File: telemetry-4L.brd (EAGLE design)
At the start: 69.8 x 22.9 mm, 70 parts, among them SW1 MF-SW-TACT-4.2MM, SW2 PCM12SMTR, U1 ATSAMD21G18A-MUT, U2 SPX3819M5-L-3-0, U3 MCP73831T-2ACI/OT, U4 IRLML6344TRPBF, U5 SIM868, U6 BMP280, U7 MPU-9250, U8 TPS61253YFFR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

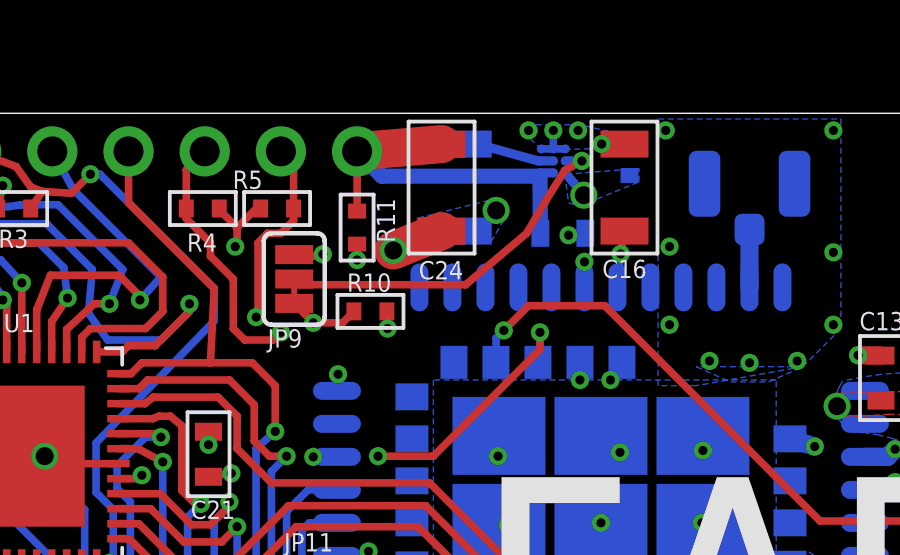
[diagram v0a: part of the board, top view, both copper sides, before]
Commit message: Killed "Servo Power 2" components
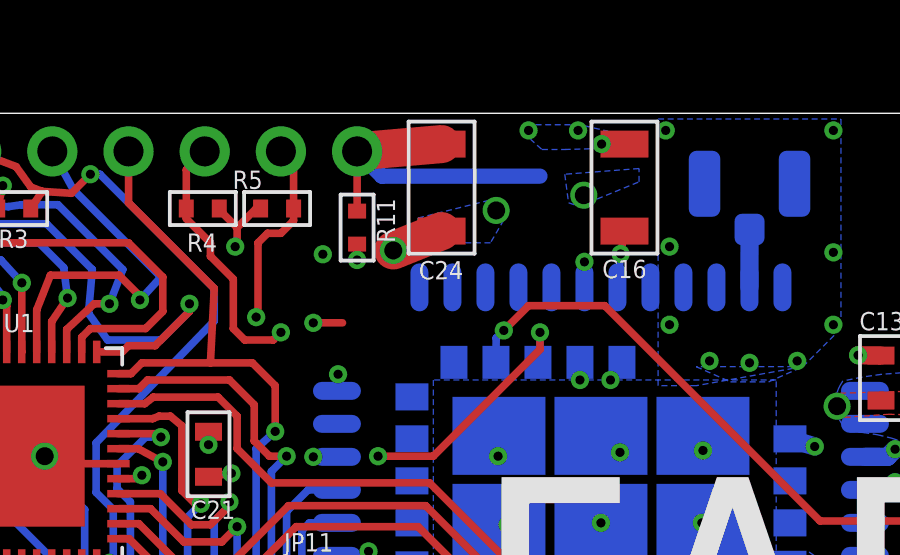
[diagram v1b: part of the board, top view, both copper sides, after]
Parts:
- removed C22: 4.7uF, MF_Passives:C0402
- removed C23: 10uF, MF_Passives:C0603
- removed JP9: JUMPER-PAD-3-2OF3_NC_BY_TRACE_SMALL, SparkFun-Passives:PAD-JUMPER-3-2OF3_NC_BY_TRACE_YES_SILK_FULL_BOX
- removed L1: 1uH, MF_Passives:L1210
- removed R10: 100K, MF_Passives:R0402
- removed U8: TPS61253YFFR, Custom:YFF9
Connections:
- removed net 5VSW: L1.P$2, U8.B1, U8.B2
- removed net 5V_EN: JP9.2, U8.B3
- net 5.0V: no longer C23.P$1, U8.A1, U8.A2
- net GND: no longer C22.P$2, C23.P$2, R10.P$1, U8.C1, U8.C2, U8.C3
- net SERVO_EN: no longer JP9.3, R10.P$2
- net VBAT_ON: no longer C22.P$1, JP9.1, L1.P$1, U8.A3
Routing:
- net 5V_EN: track 12.1 -> 0.00 mm, vias 1 -> 0
- net 5VSW: track 3.78 -> 0.00 mm
- net GND: track 119.2 -> 116.6 mm, vias 99 -> 96
- net 5.0V: track 13.7 -> 11.3 mm
- net VBAT_ON: track 60.7 -> 58.8 mm
- net SERVO_EN: track 19.8 -> 18.2 mm

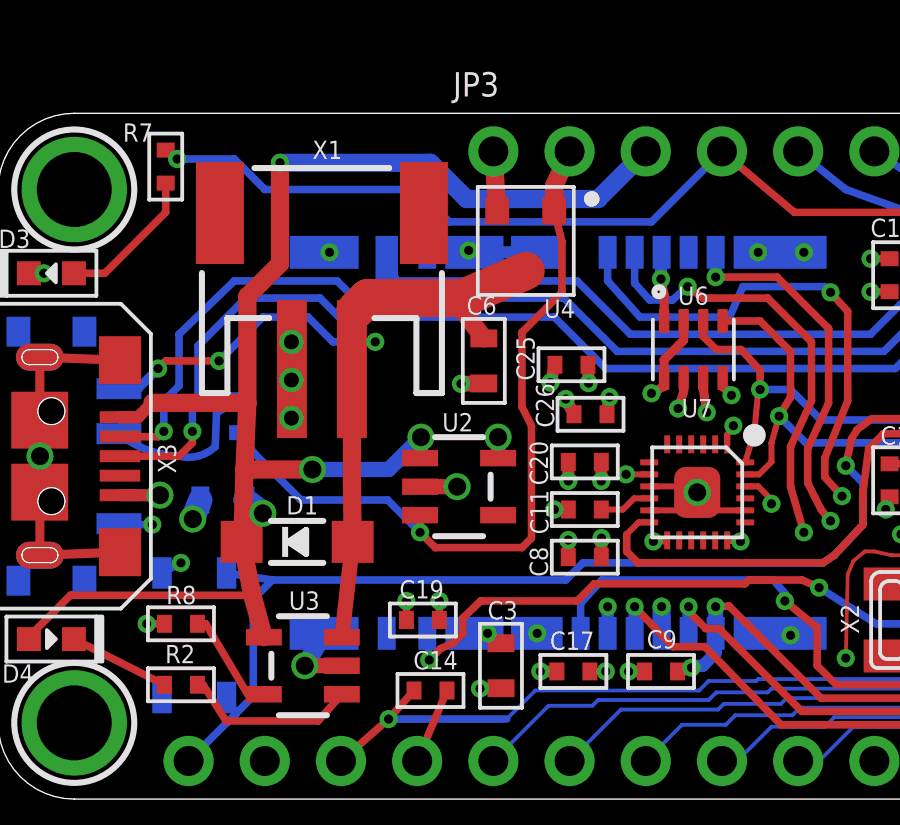
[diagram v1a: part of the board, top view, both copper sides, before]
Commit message: Swapped power FET with the one used by adafruit - Noticed the old one was the wrong way around!!
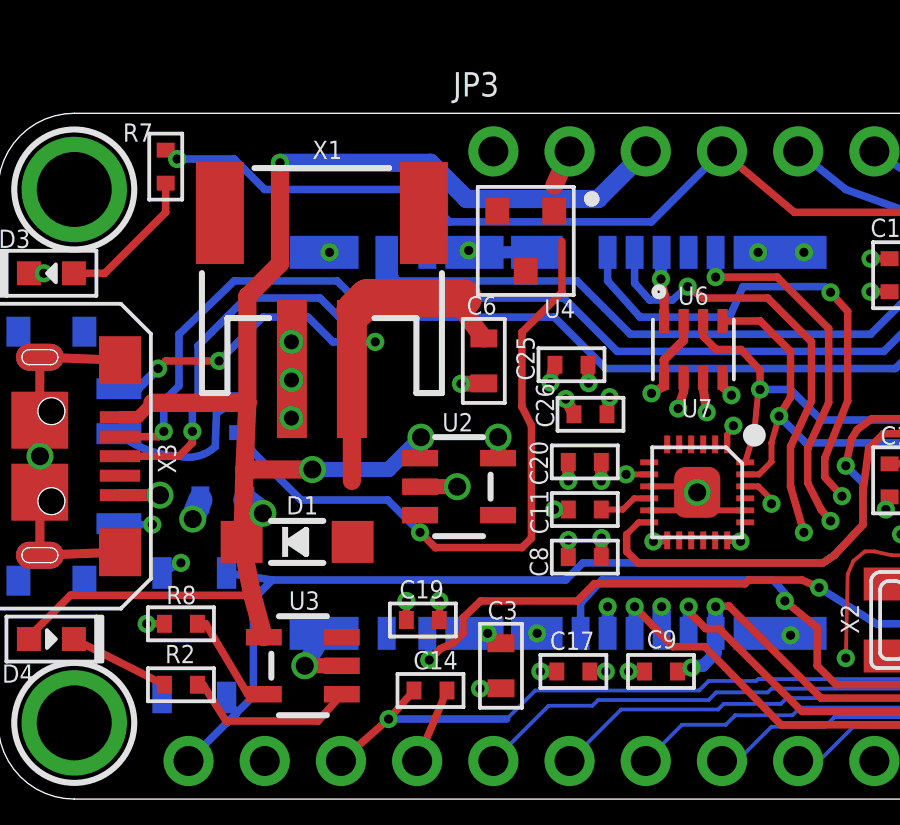
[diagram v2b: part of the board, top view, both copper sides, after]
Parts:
- U4: value IRLML6344TRPBF -> DMG3415U
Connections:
- net EN: no longer U2.3
- net VBAT: now also U4.P$2; no longer D1.A, U4.P$3
- net VBAT_ON: now also D1.A, U4.P$3; no longer U4.P$2
- net VBUS: now also U2.3
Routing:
- net VBAT: track 29.3 -> 21.8 mm
- net EN: track 25.8 -> 23.3 mm
- net VBAT_ON: track 58.8 -> 56.8 mm
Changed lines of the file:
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@@
 <layers>
 <layer number="1" name="Top" color="4" fill="1" visible="yes" active="yes"/>
-<layer number="2" name="$GND" color="1" fill="3" visible="yes" active="yes"/>
+<layer number="2" name="$GND" color="1" fill="3" visible="no" active="yes"/>
 <layer number="3" name="Route3" color="4" fill="3" visible="no" active="no"/>
 <layer number="14" name="Route14" color="1" fill="6" visible="no" active="no"/>
-<layer number="15" name="Route15" color="4" fill="6" visible="yes" active="yes"/>
+<layer number="15" name="Route15" color="4" fill="6" visible="no" active="yes"/>
 <layer number="16" name="Bottom" color="1" fill="1" visible="yes" active="yes"/>
 <layer number="17" name="Pads" color="2" fill="1" visible="yes" active="yes"/>
@@
 <attribute name="VALUE" x="-1.452" y="13.93" size="0.4064" layer="28" rot="MR90"/>
 </element>
-<element name="U4" library="MF_Discrete_Semiconductor" package="SOT-23-3" value="IRLML6344TRPBF" x="17.5895" y="18.6055" smashed="yes" rot="R270">
-<attribute name="MPN" value="" x="17.5895" y="18.6055" size="1.778" layer="27" rot="R270" display="off"/>
+<element name="U4" library="MF_Discrete_Semiconductor" package="SOT-23-3" value="DMG3415U" x="17.5895" y="18.6055" smashed="yes" rot="R270">
+<attribute name="MPN" value="DMG3415U" x="17.5895" y="18.6055" size="1.778" layer="27" rot="R270" display="off"/>
 <attribute name="HOUSEPART" value="NO" x="17.5895" y="18.6055" size="1.778" layer="27" rot="R270" display="off"/>
 <attribute name="POPULATE" value="1" x="17.5895" y="18.6055" size="1.778" layer="27" rot="R270" display="off"/>
@@
 <wire x1="10.4775" y1="10.9855" x2="8.21198125" y2="10.9855" width="0.6096" layer="1"/>
 <wire x1="8.8265" y1="9.525" x2="8.15708125" y2="9.045090625" width="0.6096" layer="1"/>
+<contactref element="U2" pad="3"/>
+<wire x1="13.02" y1="10.9855" x2="14.0669" y2="9.464" width="0" layer="19" extent="1-16"/>
 </signal>
 <signal name="VBAT">
-<contactref element="D1" pad="A"/>
 <contactref element="X1" pad="2"/>
 <contactref element="U3" pad="3"/>
 <contactref element="C6" pad="P$1"/>
-<contactref element="U4" pad="P$3"/>
 <wire x1="11.795" y1="14.334" x2="11.795" y2="14.605" width="0.8128" layer="1"/>
 <via x="5.334" y="14.351" extent="1-16" drill="0.3048"/>
@@
 <wire x1="12.319" y1="16.7005" x2="11.90625" y2="16.28775" width="1.27" layer="1"/>
 <wire x1="11.90625" y1="16.28775" x2="11.795" y2="16.1765" width="0.6096" layer="1"/>
-<wire x1="15.494" y1="16.7005" x2="17.5895" y2="17.6055" width="1.27" layer="1"/>
 <contactref element="SW2" pad="S"/>
 <wire x1="16.1925" y1="15.355" x2="15.1765" y2="16.7005" width="0.6096" layer="1"/>
 <wire x1="4.028" y1="13.68" x2="4.663" y2="13.68" width="0.3048" layer="16"/>
 <wire x1="4.663" y1="13.68" x2="5.334" y2="14.351" width="0.3048" layer="16"/>
-<wire x1="11.795" y1="10.6045" x2="11.8195" y2="8.5725" width="0.6096" layer="1"/>
 <wire x1="7.366" y1="14.605" x2="8.8265" y2="16.0655" width="0.254" layer="16"/>
 <via x="12.573" y="15.24" extent="1-16" drill="0.3048"/>
-<wire x1="11.4601" y1="5.395" x2="11.8195" y2="8.5725" width="0.508" layer="1"/>
 <wire x1="8.8265" y1="16.0655" x2="10.3345" y2="16.0655" width="0.254" layer="16"/>
 <wire x1="10.3345" y1="16.0655" x2="11.16" y2="15.24" width="0.254" layer="16"/>
 <wire x1="11.16" y1="15.24" x2="12.573" y2="15.24" width="0.254" layer="16"/>
 <wire x1="12.573" y1="15.24" x2="11.795" y2="15.24" width="0.254" layer="1"/>
+<contactref element="U4" pad="P$2"/>
+<wire x1="11.4601" y1="5.395" x2="11.795" y2="10.6045" width="0" layer="19" extent="1-1"/>
+<wire x1="15.494" y1="16.7005" x2="16.6395" y2="19.6055" width="0" layer="19" extent="1-1"/>
 </signal>
 <signal name="D13/RLED">
@@
 </signal>
 <signal name="EN">
-<contactref element="U2" pad="3"/>
 <contactref element="R1" pad="P$1"/>
-<contactref element="U4" pad="P$1"/>
 <wire x1="18.796" y1="16.891" x2="18.796" y2="18.587" width="0.254" layer="1"/>
 <contactref element="JP3" pad="2"/>
-<wire x1="18.5395" y1="19.6055" x2="18.5395" y2="20.4445" width="0.6096" layer="1"/>
 <wire x1="18.5395" y1="20.4445" x2="19.05" y2="21.59" width="0.6096" layer="1"/>
-<wire x1="18.796" y1="18.587" x2="18.5395" y2="19.6055" width="0.254" layer="1"/>
 <wire x1="18.796" y1="16.891" x2="17.4625" y2="15.5575" width="0.254" layer="1"/>
 <wire x1="17.4625" y1="15.5575" x2="17.4625" y2="13.081" width="0.254" layer="1"/>
@@
 <wire x1="8.551" y1="11.515" x2="10.0965" y2="9.9695" width="0.254" layer="16"/>
 <via x="14.0669" y="8.89" extent="1-16" drill="0.3048"/>
-<wire x1="14.0669" y1="8.89" x2="14.0669" y2="9.464" width="0.254" layer="1"/>
 <wire x1="10.0965" y1="9.9695" x2="12.9874" y2="9.9695" width="0.254" layer="16"/>
 <wire x1="12.9874" y1="9.9695" x2="14.0669" y2="8.89" width="0.254" layer="16"/>
@@
 <wire x1="17.4625" y1="8.382" x2="14.5749" y2="8.382" width="0.254" layer="1"/>
 <wire x1="14.5749" y1="8.382" x2="14.0669" y2="8.89" width="0.254" layer="1"/>
+<contactref element="U4" pad="P$1"/>
+<wire x1="18.796" y1="18.587" x2="18.5395" y2="19.6055" width="0" layer="19" extent="1-1"/>
+<wire x1="18.5395" y1="19.6055" x2="18.5395" y2="20.4445" width="0" layer="19" extent="1-1"/>
 </signal>
 <signal name="TX5/GPS_RX">
@@
 <via x="45.847" y="18.161" extent="1-16" drill="0.3048"/>
 <wire x1="45.847" y1="18.161" x2="45.7708" y2="18.0848" width="0.254" layer="1"/>
-<contactref element="U4" pad="P$2"/>
 <contactref element="U5" pad="35_"/>
 <contactref element="U5" pad="34_"/>
@@
 <wire x1="54.483" y1="16.129" x2="51.689" y2="18.923" width="1.27" layer="15"/>
 <wire x1="51.689" y1="18.923" x2="51.6255" y2="19.6215" width="1.27" layer="15"/>
-<wire x1="16.6395" y1="19.6055" x2="16.51" y2="21.59" width="0.6096" layer="1"/>
 <wire x1="17.78" y1="19.6215" x2="16.51" y2="21.59" width="1.27" layer="15"/>
 <polygon width="0.2032" layer="16" isolate="0.2032" thermals="no">
@@
 <vertex x="65.2145" y="13.589"/>
 </polygon>
+<contactref element="D1" pad="A"/>
+<contactref element="U4" pad="P$3"/>
 <wire x1="66.929" y1="13.284" x2="67.7545" y2="13.409" width="0" layer="19" extent="1-16"/>
 <wire x1="65.4304" y1="13.547" x2="66.929" y2="13.284" width="0" layer="19" extent="1-16"/>
@@
 <wire x1="62.9895" y1="13.097" x2="63.918" y2="13.6075" width="0" layer="19" extent="16-16"/>
 <wire x1="66.125" y1="10.8839" x2="66.929" y2="13.284" width="0" layer="19" extent="1-16"/>
+<wire x1="11.8195" y1="8.5725" x2="17.5895" y2="17.6055" width="0" layer="19" extent="1-1"/>
+<wire x1="17.5895" y1="17.6055" x2="17.78" y2="19.6215" width="0" layer="19" extent="1-15"/>
 </signal>
 <signal name="5.0V">

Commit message: Revert "Swapped power FET with the one used by adafruit"
This reverts commit fb89b7665746a5f81bf27fb940dbf5a3e6cbfe7e.
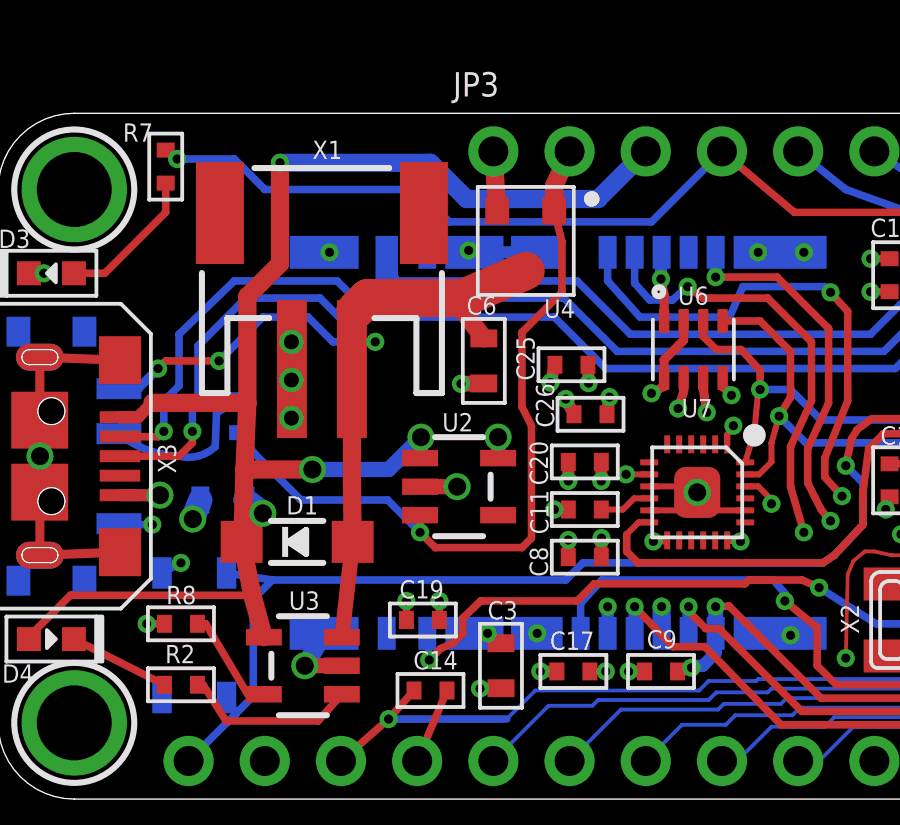
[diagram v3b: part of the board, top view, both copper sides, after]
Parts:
- U4: value DMG3415U -> IRLML6344TRPBF
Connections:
- net EN: now also U2.3
- net VBAT: now also D1.A, U4.P$3; no longer U4.P$2
- net VBAT_ON: now also U4.P$2; no longer D1.A, U4.P$3
- net VBUS: no longer U2.3
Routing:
- net VBAT: track 21.8 -> 29.3 mm
- net EN: track 23.3 -> 25.8 mm
- net VBAT_ON: track 56.8 -> 58.8 mm
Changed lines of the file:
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@@
 <layers>
 <layer number="1" name="Top" color="4" fill="1" visible="yes" active="yes"/>
-<layer number="2" name="$GND" color="1" fill="3" visible="no" active="yes"/>
+<layer number="2" name="$GND" color="1" fill="3" visible="yes" active="yes"/>
 <layer number="3" name="Route3" color="4" fill="3" visible="no" active="no"/>
 <layer number="14" name="Route14" color="1" fill="6" visible="no" active="no"/>
-<layer number="15" name="Route15" color="4" fill="6" visible="no" active="yes"/>
+<layer number="15" name="Route15" color="4" fill="6" visible="yes" active="yes"/>
 <layer number="16" name="Bottom" color="1" fill="1" visible="yes" active="yes"/>
 <layer number="17" name="Pads" color="2" fill="1" visible="yes" active="yes"/>
@@
 <attribute name="VALUE" x="-1.452" y="13.93" size="0.4064" layer="28" rot="MR90"/>
 </element>
-<element name="U4" library="MF_Discrete_Semiconductor" package="SOT-23-3" value="DMG3415U" x="17.5895" y="18.6055" smashed="yes" rot="R270">
-<attribute name="MPN" value="DMG3415U" x="17.5895" y="18.6055" size="1.778" layer="27" rot="R270" display="off"/>
+<element name="U4" library="MF_Discrete_Semiconductor" package="SOT-23-3" value="IRLML6344TRPBF" x="17.5895" y="18.6055" smashed="yes" rot="R270">
+<attribute name="MPN" value="" x="17.5895" y="18.6055" size="1.778" layer="27" rot="R270" display="off"/>
 <attribute name="HOUSEPART" value="NO" x="17.5895" y="18.6055" size="1.778" layer="27" rot="R270" display="off"/>
 <attribute name="POPULATE" value="1" x="17.5895" y="18.6055" size="1.778" layer="27" rot="R270" display="off"/>
@@
 <wire x1="10.4775" y1="10.9855" x2="8.21198125" y2="10.9855" width="0.6096" layer="1"/>
 <wire x1="8.8265" y1="9.525" x2="8.15708125" y2="9.045090625" width="0.6096" layer="1"/>
-<contactref element="U2" pad="3"/>
-<wire x1="13.02" y1="10.9855" x2="14.0669" y2="9.464" width="0" layer="19" extent="1-16"/>
 </signal>
 <signal name="VBAT">
+<contactref element="D1" pad="A"/>
 <contactref element="X1" pad="2"/>
 <contactref element="U3" pad="3"/>
 <contactref element="C6" pad="P$1"/>
+<contactref element="U4" pad="P$3"/>
 <wire x1="11.795" y1="14.334" x2="11.795" y2="14.605" width="0.8128" layer="1"/>
 <via x="5.334" y="14.351" extent="1-16" drill="0.3048"/>
@@
 <wire x1="12.319" y1="16.7005" x2="11.90625" y2="16.28775" width="1.27" layer="1"/>
 <wire x1="11.90625" y1="16.28775" x2="11.795" y2="16.1765" width="0.6096" layer="1"/>
+<wire x1="15.494" y1="16.7005" x2="17.5895" y2="17.6055" width="1.27" layer="1"/>
 <contactref element="SW2" pad="S"/>
 <wire x1="16.1925" y1="15.355" x2="15.1765" y2="16.7005" width="0.6096" layer="1"/>
 <wire x1="4.028" y1="13.68" x2="4.663" y2="13.68" width="0.3048" layer="16"/>
 <wire x1="4.663" y1="13.68" x2="5.334" y2="14.351" width="0.3048" layer="16"/>
+<wire x1="11.795" y1="10.6045" x2="11.8195" y2="8.5725" width="0.6096" layer="1"/>
 <wire x1="7.366" y1="14.605" x2="8.8265" y2="16.0655" width="0.254" layer="16"/>
 <via x="12.573" y="15.24" extent="1-16" drill="0.3048"/>
+<wire x1="11.4601" y1="5.395" x2="11.8195" y2="8.5725" width="0.508" layer="1"/>
 <wire x1="8.8265" y1="16.0655" x2="10.3345" y2="16.0655" width="0.254" layer="16"/>
 <wire x1="10.3345" y1="16.0655" x2="11.16" y2="15.24" width="0.254" layer="16"/>
 <wire x1="11.16" y1="15.24" x2="12.573" y2="15.24" width="0.254" layer="16"/>
 <wire x1="12.573" y1="15.24" x2="11.795" y2="15.24" width="0.254" layer="1"/>
-<contactref element="U4" pad="P$2"/>
-<wire x1="11.4601" y1="5.395" x2="11.795" y2="10.6045" width="0" layer="19" extent="1-1"/>
-<wire x1="15.494" y1="16.7005" x2="16.6395" y2="19.6055" width="0" layer="19" extent="1-1"/>
 </signal>
 <signal name="D13/RLED">
@@
 </signal>
 <signal name="EN">
+<contactref element="U2" pad="3"/>
 <contactref element="R1" pad="P$1"/>
+<contactref element="U4" pad="P$1"/>
 <wire x1="18.796" y1="16.891" x2="18.796" y2="18.587" width="0.254" layer="1"/>
 <contactref element="JP3" pad="2"/>
+<wire x1="18.5395" y1="19.6055" x2="18.5395" y2="20.4445" width="0.6096" layer="1"/>
 <wire x1="18.5395" y1="20.4445" x2="19.05" y2="21.59" width="0.6096" layer="1"/>
+<wire x1="18.796" y1="18.587" x2="18.5395" y2="19.6055" width="0.254" layer="1"/>
 <wire x1="18.796" y1="16.891" x2="17.4625" y2="15.5575" width="0.254" layer="1"/>
 <wire x1="17.4625" y1="15.5575" x2="17.4625" y2="13.081" width="0.254" layer="1"/>
@@
 <wire x1="8.551" y1="11.515" x2="10.0965" y2="9.9695" width="0.254" layer="16"/>
 <via x="14.0669" y="8.89" extent="1-16" drill="0.3048"/>
+<wire x1="14.0669" y1="8.89" x2="14.0669" y2="9.464" width="0.254" layer="1"/>
 <wire x1="10.0965" y1="9.9695" x2="12.9874" y2="9.9695" width="0.254" layer="16"/>
 <wire x1="12.9874" y1="9.9695" x2="14.0669" y2="8.89" width="0.254" layer="16"/>
@@
 <wire x1="17.4625" y1="8.382" x2="14.5749" y2="8.382" width="0.254" layer="1"/>
 <wire x1="14.5749" y1="8.382" x2="14.0669" y2="8.89" width="0.254" layer="1"/>
-<contactref element="U4" pad="P$1"/>
-<wire x1="18.796" y1="18.587" x2="18.5395" y2="19.6055" width="0" layer="19" extent="1-1"/>
-<wire x1="18.5395" y1="19.6055" x2="18.5395" y2="20.4445" width="0" layer="19" extent="1-1"/>
 </signal>
 <signal name="TX5/GPS_RX">
@@
 <via x="45.847" y="18.161" extent="1-16" drill="0.3048"/>
 <wire x1="45.847" y1="18.161" x2="45.7708" y2="18.0848" width="0.254" layer="1"/>
+<contactref element="U4" pad="P$2"/>
 <contactref element="U5" pad="35_"/>
 <contactref element="U5" pad="34_"/>
@@
 <wire x1="54.483" y1="16.129" x2="51.689" y2="18.923" width="1.27" layer="15"/>
 <wire x1="51.689" y1="18.923" x2="51.6255" y2="19.6215" width="1.27" layer="15"/>
+<wire x1="16.6395" y1="19.6055" x2="16.51" y2="21.59" width="0.6096" layer="1"/>
 <wire x1="17.78" y1="19.6215" x2="16.51" y2="21.59" width="1.27" layer="15"/>
 <polygon width="0.2032" layer="16" isolate="0.2032" thermals="no">
@@
 <vertex x="65.2145" y="13.589"/>
 </polygon>
-<contactref element="D1" pad="A"/>
-<contactref element="U4" pad="P$3"/>
 <wire x1="66.929" y1="13.284" x2="67.7545" y2="13.409" width="0" layer="19" extent="1-16"/>
 <wire x1="65.4304" y1="13.547" x2="66.929" y2="13.284" width="0" layer="19" extent="1-16"/>
@@
 <wire x1="62.9895" y1="13.097" x2="63.918" y2="13.6075" width="0" layer="19" extent="16-16"/>
 <wire x1="66.125" y1="10.8839" x2="66.929" y2="13.284" width="0" layer="19" extent="1-16"/>
-<wire x1="11.8195" y1="8.5725" x2="17.5895" y2="17.6055" width="0" layer="19" extent="1-1"/>
-<wire x1="17.5895" y1="17.6055" x2="17.78" y2="19.6215" width="0" layer="19" extent="1-15"/>
 </signal>
 <signal name="5.0V">
